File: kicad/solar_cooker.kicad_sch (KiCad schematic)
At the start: 3 parts, among them U1 ATmega2560-16A, U2 microSD, U3 clock_module

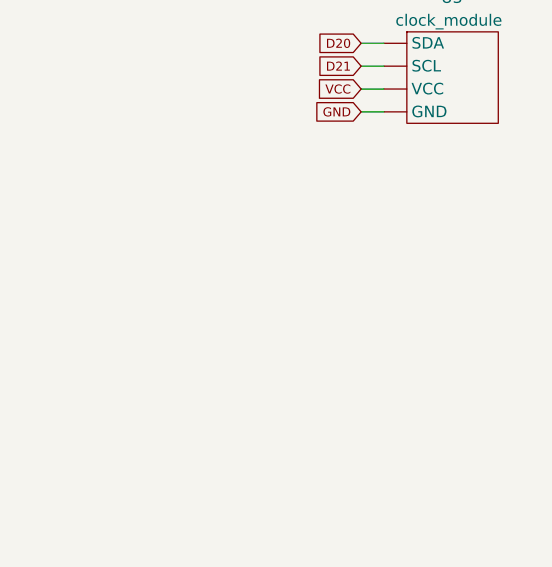
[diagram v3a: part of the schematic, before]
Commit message: added e-Paper + minor improvements
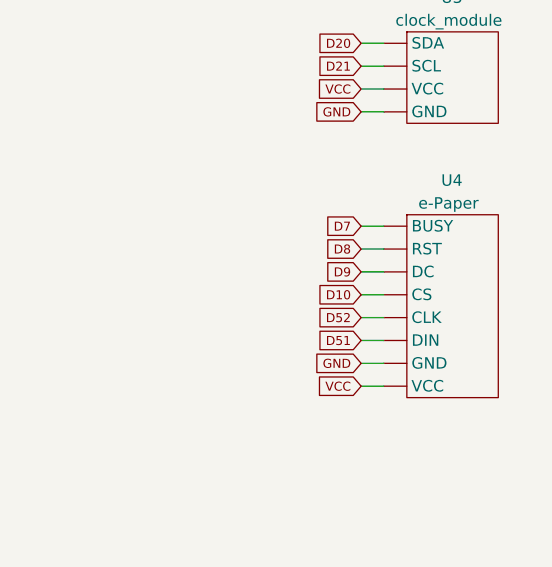
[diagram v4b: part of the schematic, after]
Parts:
- added U4: e-Paper, symbol custom_components:e-Paper
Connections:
- net D10: now also U4.4 (CS)
- net D20: now also U3.1 (SDA); no longer U3. (VCC)
- net D21: now also U3.2 (SCL); no longer U3. (VCC)
- net D4: now also U2.1 (CS); no longer U2. (VCC)
- net D50: now also U2.4 (MISO); no longer U2. (VCC)
- net D51: now also U2.3 (MOSI), U4.6 (DIN); no longer U2. (VCC)
- net D52: now also U2.2 (SCK), U4.5 (CLK); no longer U2. (VCC)
- net D7: now also U4.1 (BUSY)
- net D8: now also U4.2 (RST)
- net D9: now also U4.3 (DC)
- net GND: now also U2.6 (GND), U3.4 (GND), U4.7 (GND); no longer U2. (VCC), U3. (VCC)
- net VCC: now also U2.5 (VCC), U3.3 (VCC), U4.8 (VCC); no longer U2. (VCC), U3. (VCC)
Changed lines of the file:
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@@
+    (stroke (width 0) (type default) (color 0 0 255 1))
+  )
+  (wire (pts (xy 157.48 95.25) (xy 160.02 95.25))
     (stroke (width 0) (type default) (color 0 0 255 1))
   )
@@
     (stroke (width 0) (type default) (color 0 0 255 1))
   )
+  (wire (pts (xy 157.48 97.79) (xy 160.02 97.79))
+    (stroke (width 0) (type default) (color 0 0 0 1))
+  )
   (wire (pts (xy 85.09 59.69) (xy 87.63 59.69))
     (stroke (width 0) (type default) (color 0 0 255 1))
@@
     (stroke (width 0) (type default))
   )
+  (wire (pts (xy 157.48 100.33) (xy 160.02 100.33))
+    (stroke (width 0) (type default) (color 255 0 0 1))
+  )
   (wire (pts (xy 85.09 100.33) (xy 87.63 100.33))
     (stroke (width 0) (type default) (color 0 0 255 1))
@@
     (stroke (width 0) (type default) (color 0 0 255 1))
   )
+  (wire (pts (xy 157.48 90.17) (xy 160.02 90.17))
+    (stroke (width 0) (type default) (color 0 0 255 1))
+  )
   (wire (pts (xy 85.09 85.09) (xy 87.63 85.09))
     (stroke (width 0) (type default) (color 0 0 255 1))
@@
     (stroke (width 0) (type default))
   )
+  (wire (pts (xy 157.48 82.55) (xy 160.02 82.55))
+    (stroke (width 0) (type default) (color 0 0 255 1))
+  )
   (wire (pts (xy 41.91 133.35) (xy 44.45 133.35))
     (stroke (width 0) (type default) (color 0 0 255 1))
@@
     (stroke (width 0) (type default))
   )
+  (wire (pts (xy 157.48 92.71) (xy 160.02 92.71))
+    (stroke (width 0) (type default) (color 0 0 255 1))
+  )
   (wire (pts (xy 157.48 34.29) (xy 160.02 34.29))
     (stroke (width 0) (type default) (color 0 0 255 1))
@@
   (wire (pts (xy 85.09 146.05) (xy 87.63 146.05))
     (stroke (width 0) (type default))
+  )
+  (wire (pts (xy 157.48 87.63) (xy 160.02 87.63))
+    (stroke (width 0) (type default) (color 0 0 255 1))
   )
   (wire (pts (xy 41.91 95.25) (xy 44.45 95.25))
@@
     (stroke (width 0) (type default) (color 0 0 255 1))
   )
+  (wire (pts (xy 157.48 85.09) (xy 160.02 85.09))
+    (stroke (width 0) (type default) (color 0 0 255 1))
+  )
   (wire (pts (xy 85.09 151.13) (xy 87.63 151.13))
     (stroke (width 0) (type default))
@@
     )
   )
+  (global_label "D7" (shape input) (at 157.48 82.55 180) (fields_autoplaced)
+    (effects (font (size 1 1)) (justify right))
+    (property "Intersheetrefs" "${INTERSHEET_REFS}" (at 153.2397 82.55 0)
+      (effects (font (size 1 1)) (justify right) hide)
+    )
+  )
   (global_label "A2" (shape input) (at 87.63 151.13 0) (fields_autoplaced)
     (effects (font (size 1 1)) (justify left))
@@
     )
   )
+  (global_label "D8" (shape input) (at 157.48 85.09 180) (fields_autoplaced)
+    (effects (font (size 1 1)) (justify right))
+    (property "Intersheetrefs" "${INTERSHEET_REFS}" (at 153.2397 85.09 0)
+      (effects (font (size 1 1)) (justify right) hide)
+    )
+  )
   (global_label "D34" (shape input) (at 87.63 85.09 0) (fields_autoplaced)
     (effects (font (size 1 1)) (justify left))
@@
     )
   )
+  (global_label "GND" (shape input) (at 157.48 97.79 180) (fields_autoplaced)
+    (effects (font (size 1 1)) (justify right))
+    (property "Intersheetrefs" "${INTERSHEET_REFS}" (at 152.5324 97.7275 0)
+      (effects (font (size 1 1)) (justify right) hide)
+    )
+  )
+  (global_label "VCC" (shape input) (at 157.48 100.33 180) (fields_autoplaced)
+    (effects (font (size 1 1)) (justify right))
+    (property "Intersheetrefs" "${INTERSHEET_REFS}" (at 152.7229 100.2675 0)
+      (effects (font (size 1 1)) (justify right) hide)
+    )
+  )
   (global_label "D5" (shape input) (at 87.63 130.81 0) (fields_autoplaced)
     (effects (font (size 1 1)) (justify left))
@@
   )
   (global_label "D51" (shape input) (at 157.48 39.37 180) (fields_autoplaced)
-    (effects (font (size 1 1)) (justify right))
-    (property "Intersheetrefs" "${INTERSHEET_REFS}" (at 152.6752 39.3075 0)
+    (effects (font (size 1 1) (color 255 0 0 1)) (justify right))
+    (property "Intersheetrefs" "${INTERSHEET_REFS}" (at 152.2873 39.37 0)
       (effects (font (size 1 1)) (justify right) hide)
     )
@@
   )
   (global_label "D52" (shape input) (at 157.48 36.83 180) (fields_autoplaced)
-    (effects (font (size 1 1)) (justify right))
-    (property "Intersheetrefs" "${INTERSHEET_REFS}" (at 152.6752 36.7675 0)
+    (effects (font (size 1 1) (color 255 0 0 1)) (justify right))
+    (property "Intersheetrefs" "${INTERSHEET_REFS}" (at 152.2873 36.83 0)
       (effects (font (size 1 1)) (justify right) hide)
     )
@@
   (global_label "D49" (shape input) (at 41.91 54.61 180) (fields_autoplaced)
     (effects (font (size 1 1)) (justify right))
-    (property "Intersheetrefs" "${INTERSHEET_REFS}" (at 37.1052 54.5475 0)
+    (property "Intersheetrefs" "${INTERSHEET_REFS}" (at 36.7173 54.61 0)
       (effects (font (size 1 1)) (justify right) hide)
     )
@@
     )
   )
+  (global_label "D10" (shape input) (at 157.48 90.17 180) (fields_autoplaced)
+    (effects (font (size 1 1)) (justify right))
+    (property "Intersheetrefs" "${INTERSHEET_REFS}" (at 152.2873 90.17 0)
+      (effects (font (size 1 1)) (justify right) hide)
+    )
+  )
   (global_label "A1" (shape input) (at 87.63 148.59 0) (fields_autoplaced)
     (effects (font (size 1 1)) (justify left))
@@
     )
   )
+  (global_label "D52" (shape input) (at 157.48 92.71 180) (fields_autoplaced)
+    (effects (font (size 1 1) (color 255 0 0 1)) (justify right))
+    (property "Intersheetrefs" "${INTERSHEET_REFS}" (at 152.2873 92.71 0)
+      (effects (font (size 1 1)) (justify right) hide)
+    )
+  )
   (global_label "D2" (shape input) (at 87.63 133.35 0) (fields_autoplaced)
     (effects (font (size 1 1)) (justify left))
@@
     )
   )
+  (global_label "D9" (shape input) (at 157.48 87.63 180) (fields_autoplaced)
+    (effects (font (size 1 1)) (justify right))
+    (property "Intersheetrefs" "${INTERSHEET_REFS}" (at 153.2397 87.63 0)
+      (effects (font (size 1 1)) (justify right) hide)
+    )
+  )
   (global_label "GND" (shape input) (at 157.48 46.99 180) (fields_autoplaced)
     (effects (font (size 1 1)) (justify right))
@@
     (property "Intersheetrefs" "${INTERSHEET_REFS}" (at 92.4348 62.1675 0)
       (effects (font (size 1 1)) (justify left) hide)
+    )
+  )
+  (global_label "D51" (shape input) (at 157.48 95.25 180) (fields_autoplaced)
+    (effects (font (size 1 1) (color 255 0 0 1)) (justify right))
+    (property "Intersheetrefs" "${INTERSHEET_REFS}" (at 152.2873 95.25 0)
+      (effects (font (size 1 1)) (justify right) hide)
     )
   )
@@
       (effects (font (size 1.27 1.27)) hide)
     )
-    (pin "")
-    (pin "")
-    (pin "")
-    (pin "")
-    (pin "")
-    (pin "")
+    (pin "1")
+    (pin "2")
+    (pin "3")
+    (pin "4")
+    (pin "5")
+    (pin "6")
     (instances
       (project "solar_cooker"
@@
     )
   )
+  (symbol (lib_id "custom_components:e-Paper") (at 167.64 91.44 0) (unit 1)
+    (in_bom yes) (on_board yes) (dnp no)
+    (property "Reference" "U4" (at 166.37 77.47 0)
+      (effects (font (size 1.27 1.27)) (justify left))
+    )
+    (property "Value" "e-Paper" (at 163.83 80.01 0)
+      (effects (font (size 1.27 1.27)) (justify left))
+    )
+    (property "Footprint" "" (at 168.91 91.44 0)
+      (effects (font (size 1.27 1.27)) hide)
+    )
+    (property "Datasheet" "" (at 168.91 91.44 0)
+      (effects (font (size 1.27 1.27)) hide)
+    )
+    (pin "1")
+    (pin "2")
+    (pin "3")
+    (pin "4")
+    (pin "5")
+    (pin "6")
+    (pin "7")
+    (pin "8")
+    (instances
+      (project "solar_cooker"
+        (path "/61392a14-41f9-4325-aa01-94abd722c473"
+          (reference "U4") (unit 1)
+        )
+      )
+    )
+  )
   (symbol (lib_id "custom_components:clock_module") (at 167.64 66.04 0) (unit 1)
     (in_bom yes) (on_board yes) (dnp no)
@@
       (effects (font (size 1.27 1.27)) hide)
     )
-    (pin "")
-    (pin "")
-    (pin "")
-    (pin "")
+    (pin "1")
+    (pin "2")
+    (pin "3")
+    (pin "4")
     (instances
       (project "solar_cooker"

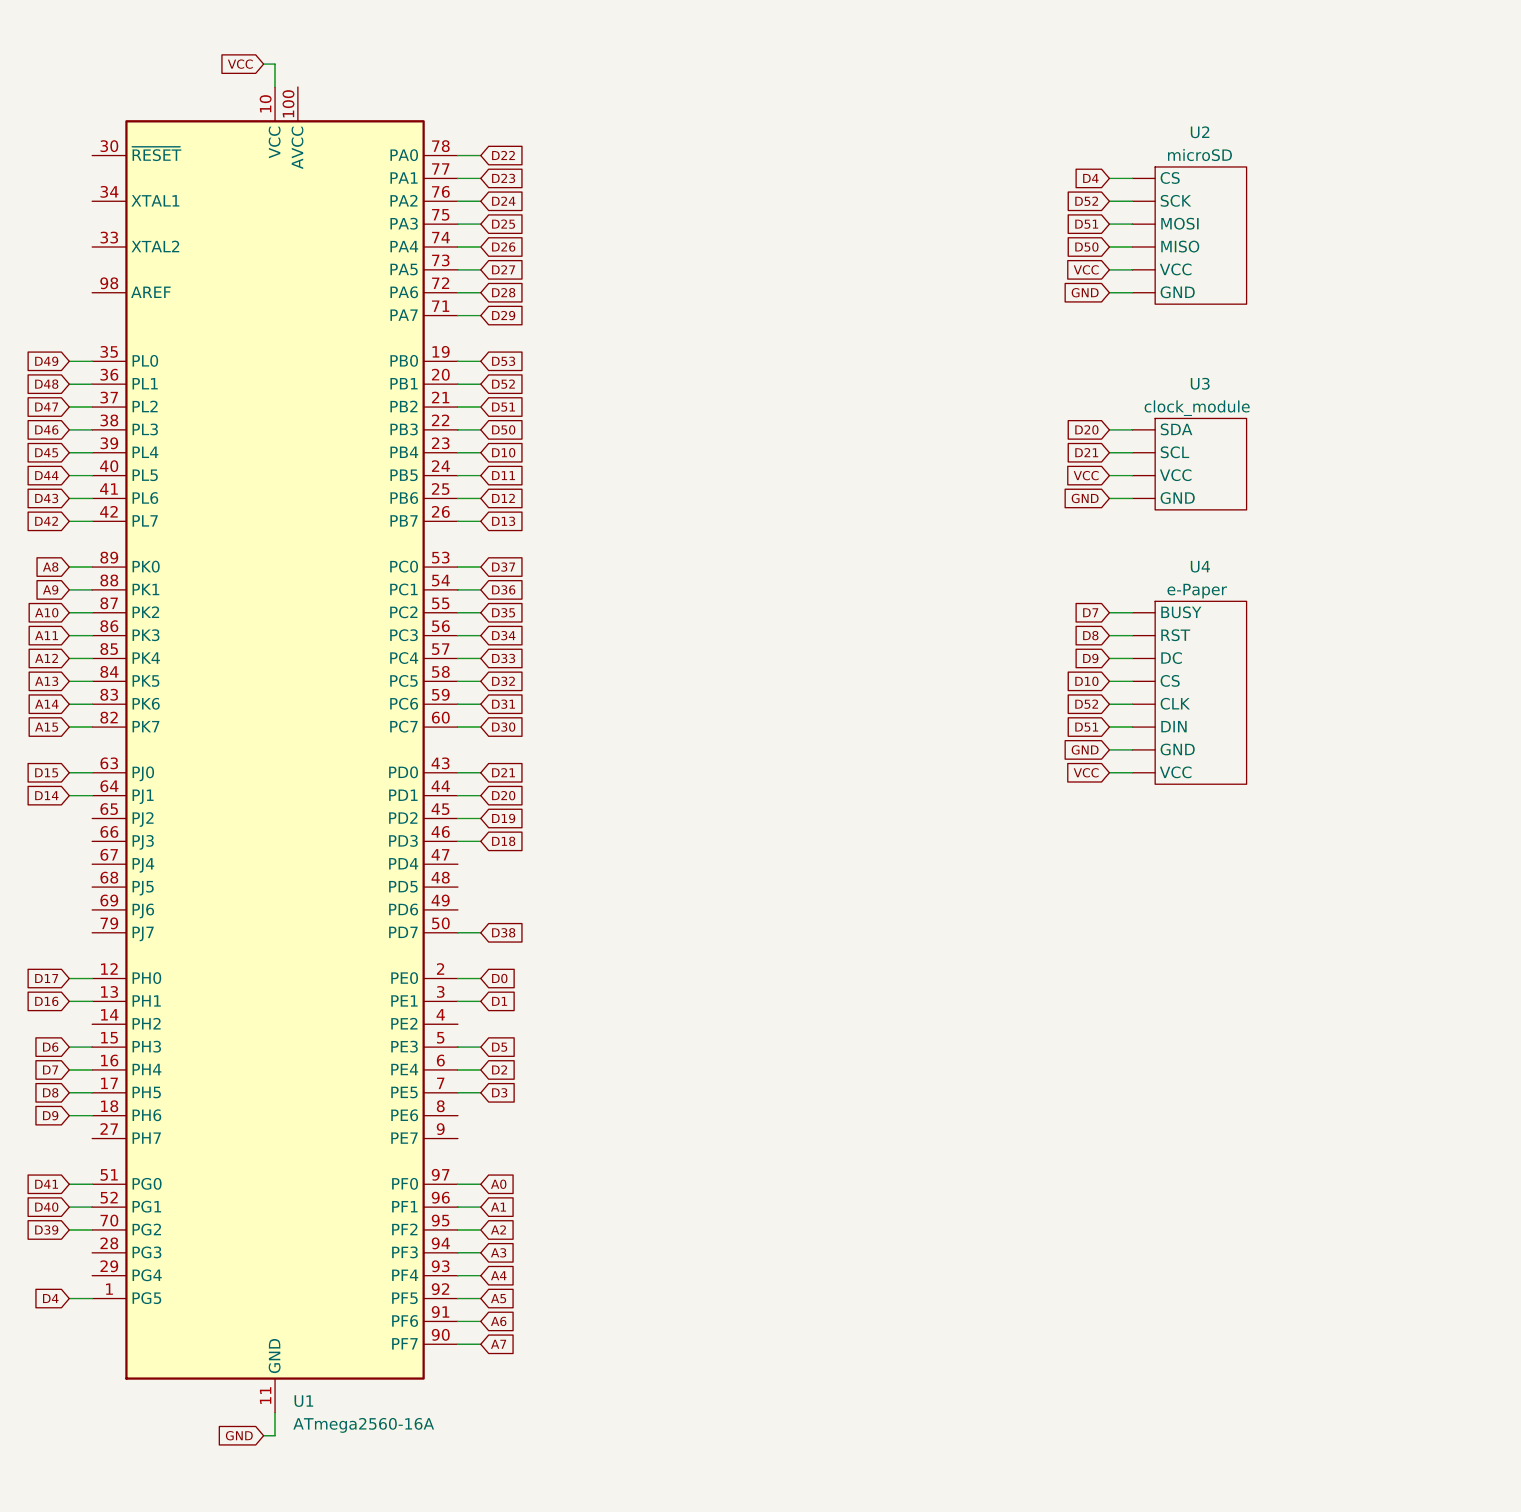
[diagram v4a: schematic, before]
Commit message: anemometer + switch schematic
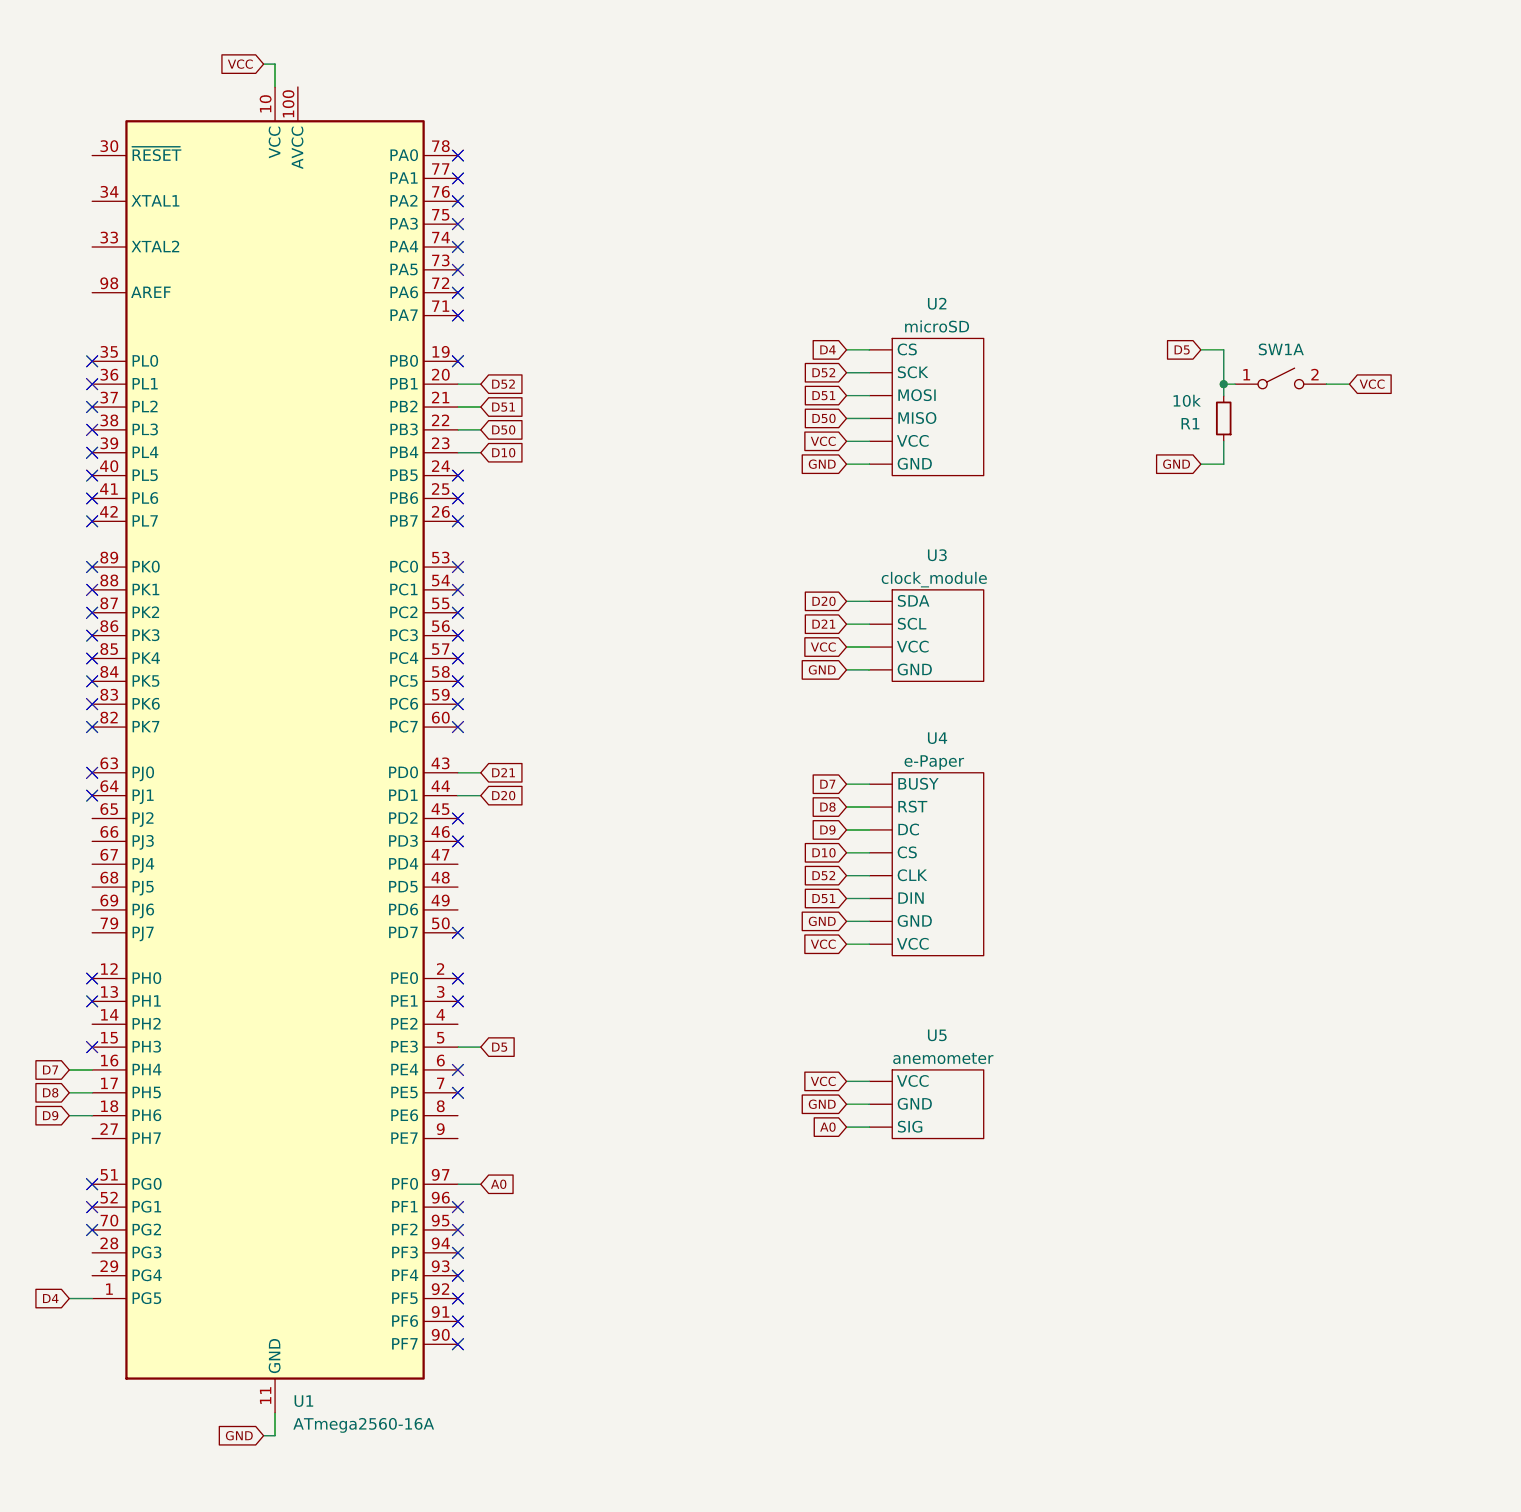
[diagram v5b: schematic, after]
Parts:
- added R1: 10k, symbol Device:R_Small
- added SW1: ~, symbol Switch:SW_DPST_x2
- added U5: anemometer, symbol custom_components:anemometer
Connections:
- net A0: now also U5.3 (SIG)
- net D5: now also R1.2, SW1.1 (A)
- net GND: now also R1.1, U5.2 (GND)
- net VCC: now also SW1.2 (B), U5.1 (VCC)
- net A1: no longer names the net of U1.96 (PF1)
- net A10: no longer names the net of U1.87 (PK2)
- net A11: no longer names the net of U1.86 (PK3)
- net A12: no longer names the net of U1.85 (PK4)
- net A13: no longer names the net of U1.84 (PK5)
- net A14: no longer names the net of U1.83 (PK6)
- net A15: no longer names the net of U1.82 (PK7)
- net A2: no longer names the net of U1.95 (PF2)
- net A3: no longer names the net of U1.94 (PF3)
- net A4: no longer names the net of U1.93 (PF4)
- net A5: no longer names the net of U1.92 (PF5)
- net A6: no longer names the net of U1.91 (PF6)
- net A7: no longer names the net of U1.90 (PF7)
- net A8: no longer names the net of U1.89 (PK0)
- net A9: no longer names the net of U1.88 (PK1)
- net D0: no longer names the net of U1.2 (PE0)
- net D1: no longer names the net of U1.3 (PE1)
- net D11: no longer names the net of U1.24 (PB5)
- net D12: no longer names the net of U1.25 (PB6)
- net D13: no longer names the net of U1.26 (PB7)
- net D14: no longer names the net of U1.64 (PJ1)
- net D15: no longer names the net of U1.63 (PJ0)
- net D16: no longer names the net of U1.13 (PH1)
- net D17: no longer names the net of U1.12 (PH0)
- net D18: no longer names the net of U1.46 (PD3)
- net D19: no longer names the net of U1.45 (PD2)
- net D2: no longer names the net of U1.6 (PE4)
- net D22: no longer names the net of U1.78 (PA0)
- net D23: no longer names the net of U1.77 (PA1)
- net D24: no longer names the net of U1.76 (PA2)
- net D25: no longer names the net of U1.75 (PA3)
- net D26: no longer names the net of U1.74 (PA4)
- net D27: no longer names the net of U1.73 (PA5)
- net D28: no longer names the net of U1.72 (PA6)
- net D29: no longer names the net of U1.71 (PA7)
- net D3: no longer names the net of U1.7 (PE5)
- net D30: no longer names the net of U1.60 (PC7)
- net D31: no longer names the net of U1.59 (PC6)
- net D32: no longer names the net of U1.58 (PC5)
- net D33: no longer names the net of U1.57 (PC4)
- net D34: no longer names the net of U1.56 (PC3)
- net D35: no longer names the net of U1.55 (PC2)
- net D36: no longer names the net of U1.54 (PC1)
- net D37: no longer names the net of U1.53 (PC0)
- net D38: no longer names the net of U1.50 (PD7)
- net D39: no longer names the net of U1.70 (PG2)
- net D40: no longer names the net of U1.52 (PG1)
- net D41: no longer names the net of U1.51 (PG0)
- net D42: no longer names the net of U1.42 (PL7)
- net D43: no longer names the net of U1.41 (PL6)
- net D44: no longer names the net of U1.40 (PL5)
- net D45: no longer names the net of U1.39 (PL4)
- net D46: no longer names the net of U1.38 (PL3)
- net D47: no longer names the net of U1.37 (PL2)
- net D48: no longer names the net of U1.36 (PL1)
- net D49: no longer names the net of U1.35 (PL0)
- net D53: no longer names the net of U1.19 (PB0)
- net D6: no longer names the net of U1.15 (PH3)
- no-connect marks 0 -> 58
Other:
- moved on the sheet: U2, U3, U4
